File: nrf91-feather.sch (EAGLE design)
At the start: 93 parts, among them J2 CON-HEADER-1X12-MALE-PIN, J3 CON-HEADER-1X16-MALE-PIN, J4 CON-1909763-1, J5 CON-SIM-104224-0820, J6 CON-S2B-PH-SM4-TB(LF)(SN), J7 CON-1909763-1, J8 CON-USB-DX07S016JA1R1500, J9 CON-TC2030-MCP-NL, Q2 MOSFET-DUAL-COMP-SOT563, Q3 MOSFET-P-20V-4.7A-SOT23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

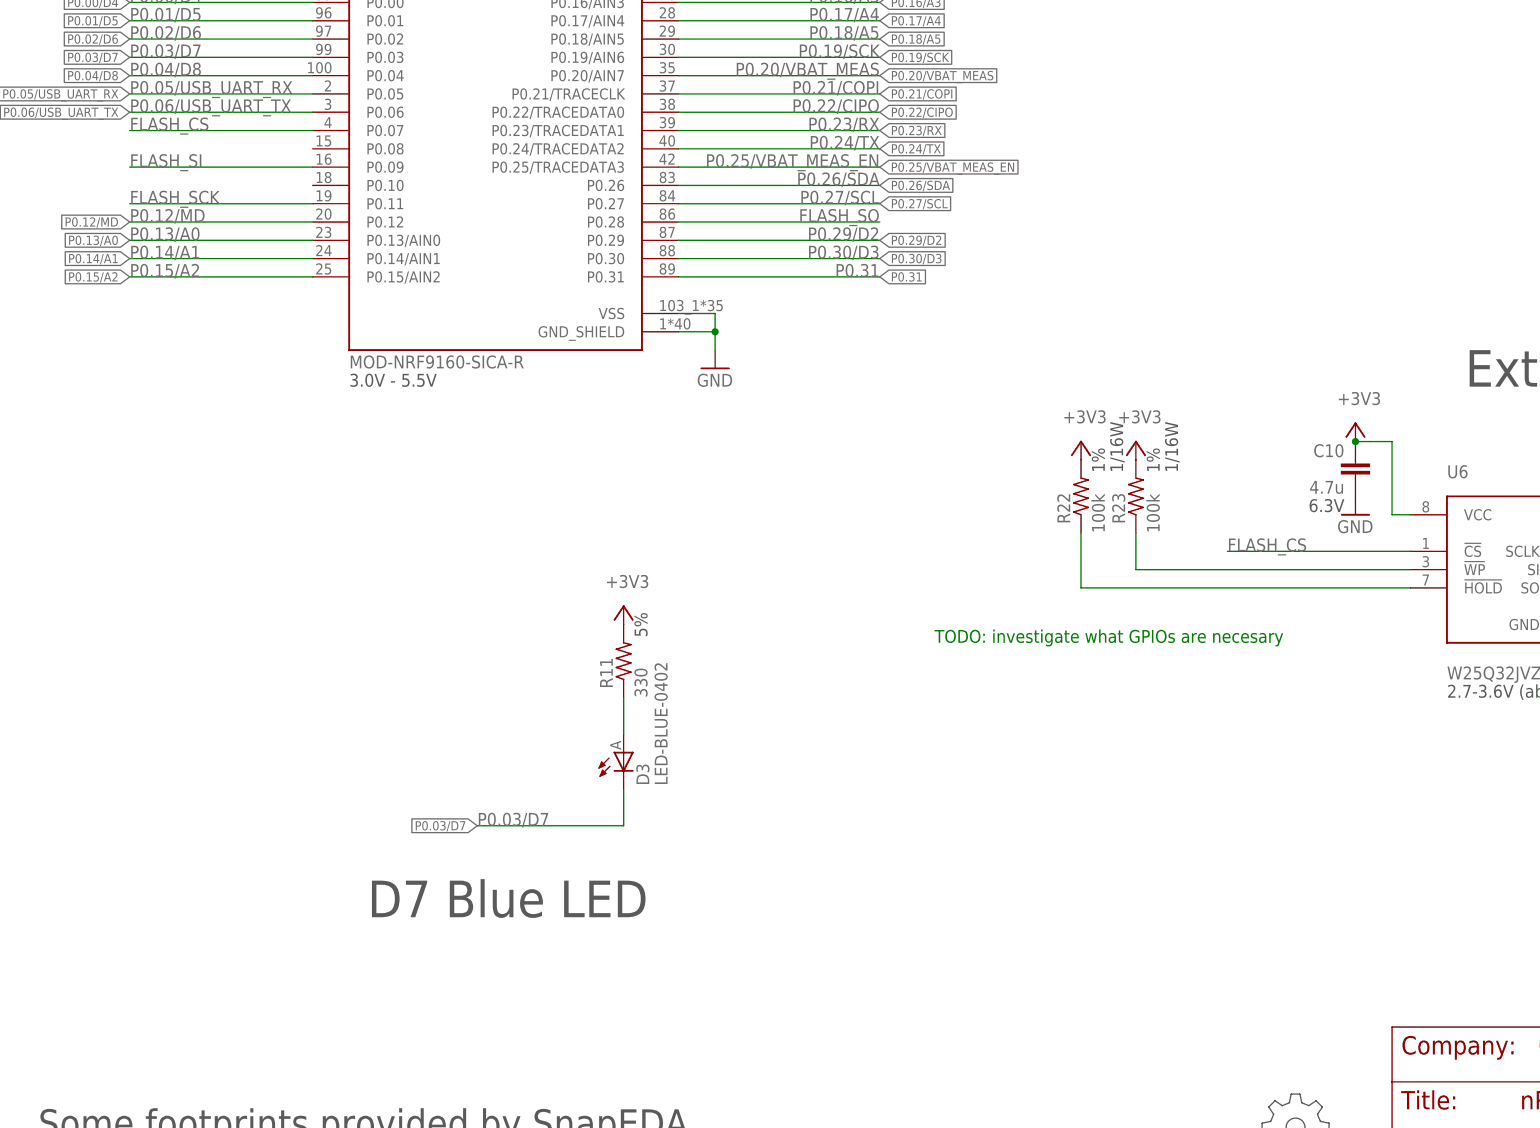
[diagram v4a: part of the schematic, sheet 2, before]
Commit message: Reconnect flash signals
Changed:
* Reconnect WP and HOLD signls
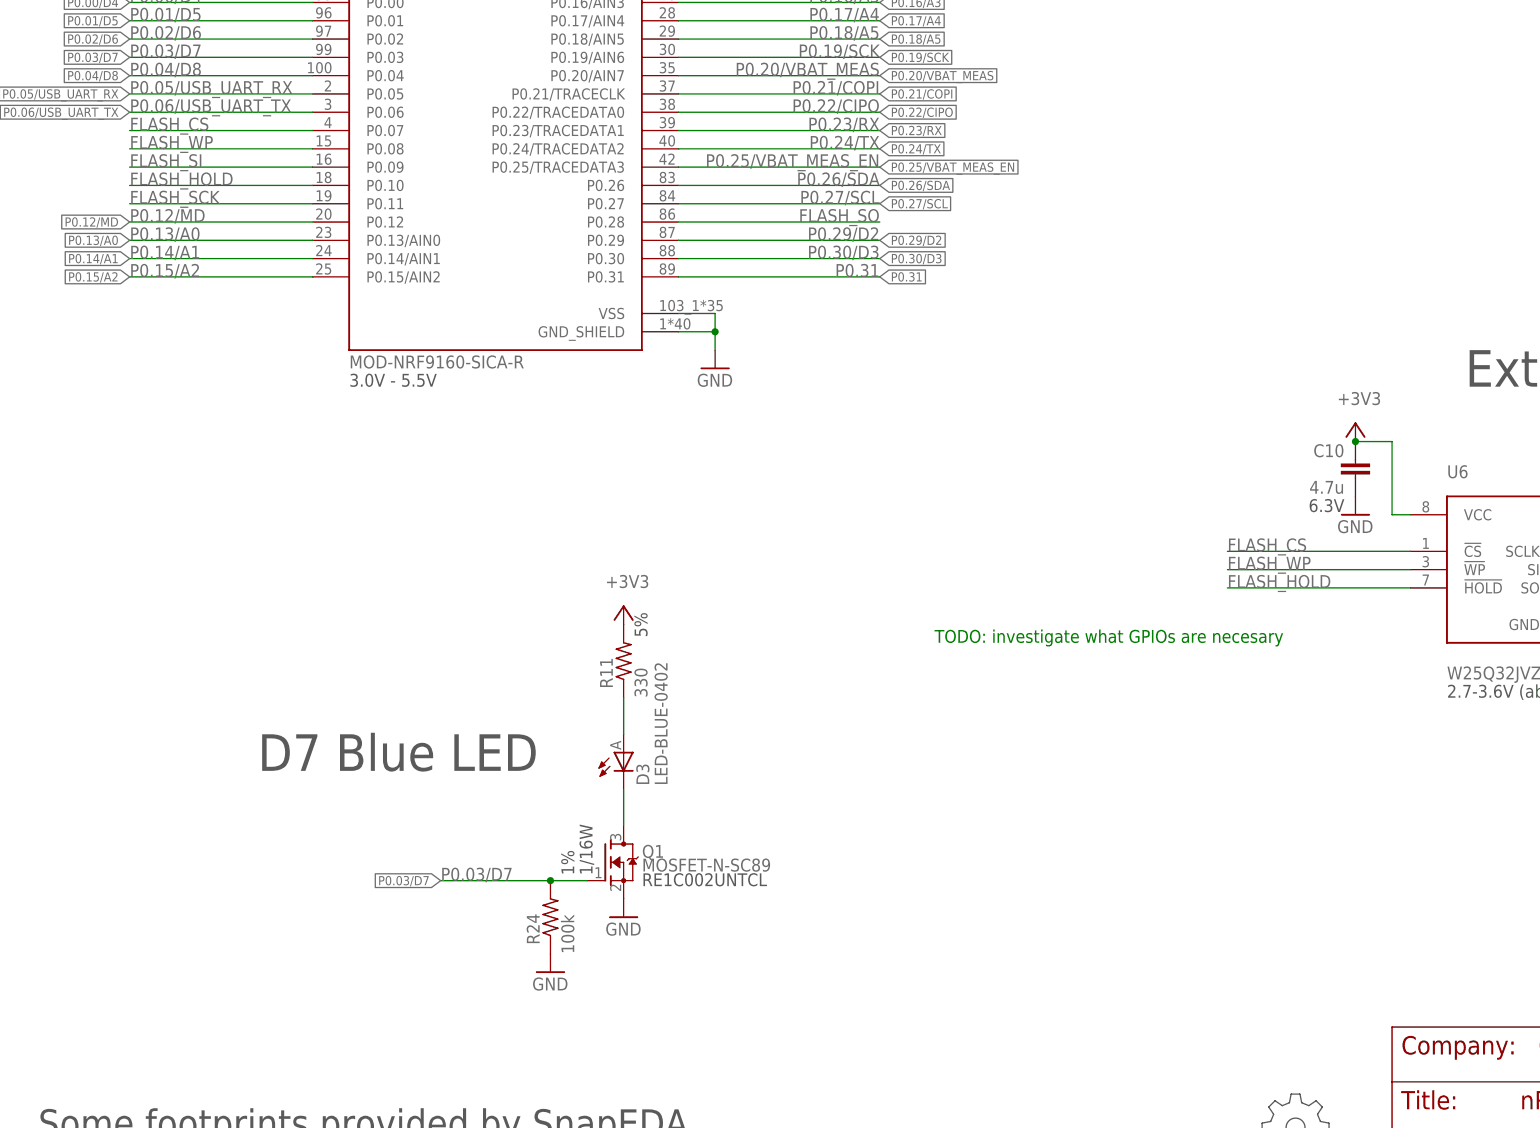
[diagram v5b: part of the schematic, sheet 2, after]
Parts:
- removed R22, R23: 100k, wolff-den:RES-100K-1%-0402
- added Q1: MOSFET-N-SC89, wolff-den:MOSFET-N-SC89
- added R24: 100k, wolff-den:RES-100K-1%-0402
- R19: value 1M -> 100k; device wolff-den:RES-1M-5%-0402 -> wolff-den:RES-100K-1%-0402
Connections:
- removed net N$14: R22.1, U6.!HOLD
- removed net N$9: R23.1, U6.!WP
- new net FLASH_HOLD: U1.P0.10, U6.!HOLD
- new net FLASH_WP: U1.P0.08, U6.!WP
- new net N$12: D3.C, Q1.D
- net +3V3: no longer R22.2, R23.2
- net GND: now also Q1.S, R24.1
- net P0.03/D7: now also Q1.G, R24.2; no longer D3.C
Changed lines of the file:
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@@
 <attribute name="MQTY" value="150"/>
 </part>
-<part name="R19" library="wolff-den" library_urn="urn:adsk.eagle:library:6370453" deviceset="RES" device="-0402" package3d_urn="urn:adsk.eagle:package:19061974/5" technology="-1M-5%" value="1M"/>
+<part name="R19" library="wolff-den" library_urn="urn:adsk.eagle:library:6370453" deviceset="RES" device="-0402" package3d_urn="urn:adsk.eagle:package:19061974/5" technology="-100K-1%" value="100k"/>
 <part name="U4" library="wolff-den" library_urn="urn:adsk.eagle:library:6370453" deviceset="POWER-SWITCH" device="-DFN4" override_package3d_urn="urn:adsk.eagle:package:36693341/2" override_package_urn="urn:adsk.eagle:footprint:36693342/1" technology="-SIP32409" value="POWER-SWITCH-SIP32409-DFN4"/>
 <part name="GND27" library="supply1" library_urn="urn:adsk.eagle:library:371" deviceset="GND" device=""/>
@@
 <part name="C6" library="wolff-den" library_urn="urn:adsk.eagle:library:6370453" deviceset="CAP" device="-0402" package3d_urn="urn:adsk.eagle:package:7419912/7" technology="-1U-25V-1" value="1u"/>
 <part name="GND47" library="supply1" library_urn="urn:adsk.eagle:library:371" deviceset="GND" device=""/>
-<part name="R22" library="wolff-den" library_urn="urn:adsk.eagle:library:6370453" deviceset="RES" device="-0402" package3d_urn="urn:adsk.eagle:package:19061974/5" technology="-100K-1%" value="100k"/>
-<part name="R23" library="wolff-den" library_urn="urn:adsk.eagle:library:6370453" deviceset="RES" device="-0402" package3d_urn="urn:adsk.eagle:package:19061974/5" technology="-100K-1%" value="100k"/>
-<part name="+3V10" library="supply1" library_urn="urn:adsk.eagle:library:371" deviceset="+3V3" device=""/>
-<part name="+3V14" library="supply1" library_urn="urn:adsk.eagle:library:371" deviceset="+3V3" device=""/>
 <part name="C3" library="wolff-den" library_urn="urn:adsk.eagle:library:6370453" deviceset="CAP" device="-0805" package3d_urn="urn:adsk.eagle:package:5807330/7" technology="-47U-6.3V" value="47u"/>
 <part name="GND11" library="supply1" library_urn="urn:adsk.eagle:library:371" deviceset="GND" device=""/>
@@
 <part name="R5" library="wolff-den" library_urn="urn:adsk.eagle:library:6370453" deviceset="RES" device="-0402" package3d_urn="urn:adsk.eagle:package:19061974/5" technology="-100K-1%" value="100k"/>
 <part name="GND32" library="supply1" library_urn="urn:adsk.eagle:library:371" deviceset="GND" device=""/>
+<part name="Q1" library="wolff-den" library_urn="urn:adsk.eagle:library:6370453" deviceset="MOSFET-N" device="-SC89" package3d_urn="urn:adsk.eagle:package:19061973/4"/>
+<part name="GND37" library="supply1" library_urn="urn:adsk.eagle:library:371" deviceset="GND" device=""/>
+<part name="R24" library="wolff-den" library_urn="urn:adsk.eagle:library:6370453" deviceset="RES" device="-0402" package3d_urn="urn:adsk.eagle:package:19061974/5" technology="-100K-1%" value="100k"/>
+<part name="GND48" library="supply1" library_urn="urn:adsk.eagle:library:371" deviceset="GND" device=""/>
 </parts>
 <sheets>
@@
 <text x="63.5" y="88.9" size="5.08" layer="97">Buttons</text>
 <text x="332.74" y="119.38" size="5.08" layer="97">External Flash</text>
-<text x="180.34" y="45.72" size="5.08" layer="97">D7 Blue LED</text>
+<text x="165.1" y="66.04" size="5.08" layer="97">D7 Blue LED</text>
 <text x="177.8" y="119.38" size="1.778" layer="97">3.0V - 5.5V</text>
 <text x="330.2" y="76.2" size="1.778" layer="97">2.7-3.6V (abs max 4.6)</text>
@@
 <attribute name="VALUE" x="248.92" y="208.28" size="1.778" layer="96" rot="MR0"/>
 </instance>
-<instance part="R22" gate="G$1" x="279.4" y="104.14" smashed="yes" rot="R90">
-<attribute name="NAME" x="277.9014" y="100.33" size="1.778" layer="95" rot="R90"/>
-<attribute name="VALUE" x="282.702" y="99.06" size="1.778" layer="96" rot="R90"/>
-<attribute name="TOLERANCE" x="282.702" y="107.442" size="1.778" layer="97" rot="R90"/>
-<attribute name="POWER" x="285.242" y="107.442" size="1.778" layer="97" rot="R90"/>
-</instance>
-<instance part="R23" gate="G$1" x="287.02" y="104.14" smashed="yes" rot="R90">
-<attribute name="NAME" x="285.5214" y="100.33" size="1.778" layer="95" rot="R90"/>
-<attribute name="VALUE" x="290.322" y="99.06" size="1.778" layer="96" rot="R90"/>
-<attribute name="TOLERANCE" x="290.322" y="107.442" size="1.778" layer="97" rot="R90"/>
-<attribute name="POWER" x="292.862" y="107.442" size="1.778" layer="97" rot="R90"/>
-</instance>
-<instance part="+3V10" gate="G$1" x="287.02" y="111.76" smashed="yes">
-<attribute name="VALUE" x="284.48" y="114.3" size="1.778" layer="96"/>
-</instance>
-<instance part="+3V14" gate="G$1" x="279.4" y="111.76" smashed="yes">
-<attribute name="VALUE" x="276.86" y="114.3" size="1.778" layer="96"/>
-</instance>
 <instance part="C3" gate="A" x="241.3" y="238.76" smashed="yes">
 <attribute name="NAME" x="242.824" y="239.141" size="1.778" layer="95"/>
@@
 <attribute name="NAME" x="148.59" y="240.1316" size="1.778" layer="95"/>
 </instance>
+<instance part="Q1" gate="A" x="213.36" y="53.34" smashed="yes">
+<attribute name="NAME" x="218.44" y="53.975" size="1.778" layer="95"/>
+<attribute name="VALUE" x="218.44" y="52.07" size="1.778" layer="96"/>
+<attribute name="MPN" x="218.44" y="50.038" size="1.778" layer="97" ratio="6"/>
+</instance>
+<instance part="GND37" gate="1" x="215.9" y="45.72" smashed="yes">
+<attribute name="VALUE" x="213.36" y="43.18" size="1.778" layer="96"/>
+</instance>
+<instance part="R24" gate="G$1" x="205.74" y="45.72" smashed="yes" rot="R90">
+<attribute name="NAME" x="204.2414" y="41.91" size="1.778" layer="95" rot="R90"/>
+<attribute name="VALUE" x="209.042" y="40.64" size="1.778" layer="96" rot="R90"/>
+<attribute name="TOLERANCE" x="209.042" y="51.562" size="1.778" layer="97" rot="R90"/>
+<attribute name="POWER" x="211.582" y="51.562" size="1.778" layer="97" rot="R90"/>
+</instance>
+<instance part="GND48" gate="1" x="205.74" y="38.1" smashed="yes">
+<attribute name="VALUE" x="203.2" y="35.56" size="1.778" layer="96"/>
+</instance>
 </instances>
 <busses>
@@
 <pinref part="GND51" gate="1" pin="GND"/>
 </segment>
+<segment>
+<pinref part="Q1" gate="A" pin="S"/>
+<pinref part="GND37" gate="1" pin="GND"/>
+</segment>
+<segment>
+<pinref part="R24" gate="G$1" pin="1"/>
+<pinref part="GND48" gate="1" pin="GND"/>
+</segment>
 </net>
 <net name="P0.12/MD" class="0">
@@
 </segment>
 <segment>
-<pinref part="R23" gate="G$1" pin="2"/>
-<pinref part="+3V10" gate="G$1" pin="+3V3"/>
-</segment>
-<segment>
-<pinref part="R22" gate="G$1" pin="2"/>
-<pinref part="+3V14" gate="G$1" pin="+3V3"/>
-</segment>
-<segment>
 <pinref part="U1" gate="G$1" pin="VDD2"/>
 <wire x1="223.52" y1="228.6" x2="228.6" y2="228.6" width="0.1524" layer="91"/>
@@
 <net name="P0.03/D7" class="0">
 <segment>
-<wire x1="195.58" y1="58.42" x2="215.9" y2="58.42" width="0.1524" layer="91"/>
-<label x="195.58" y="58.42" size="1.778" layer="95"/>
-<label x="195.58" y="58.42" size="1.27" layer="95" rot="MR0" xref="yes"/>
-<pinref part="D3" gate="G$1" pin="C"/>
-<wire x1="215.9" y1="63.5" x2="215.9" y2="58.42" width="0.1524" layer="91"/>
+<label x="190.5" y="50.8" size="1.778" layer="95"/>
+<label x="190.5" y="50.8" size="1.27" layer="95" rot="MR0" xref="yes"/>
+<wire x1="190.5" y1="50.8" x2="205.74" y2="50.8" width="0.1524" layer="91"/>
+<pinref part="R24" gate="G$1" pin="2"/>
+<pinref part="Q1" gate="A" pin="G"/>
+<wire x1="205.74" y1="50.8" x2="210.82" y2="50.8" width="0.1524" layer="91"/>
+<junction x="205.74" y="50.8"/>
 </segment>
 <segment>
@@
 </segment>
 </net>
-<net name="N$9" class="0">
-<segment>
-<pinref part="U6" gate="G$1" pin="!WP"/>
-<pinref part="R23" gate="G$1" pin="1"/>
-<wire x1="325.12" y1="93.98" x2="287.02" y2="93.98" width="0.1524" layer="91"/>
-<wire x1="287.02" y1="93.98" x2="287.02" y2="99.06" width="0.1524" layer="91"/>
-</segment>
-</net>
-<net name="N$14" class="0">
-<segment>
-<pinref part="U6" gate="G$1" pin="!HOLD"/>
-<pinref part="R22" gate="G$1" pin="1"/>
-<wire x1="325.12" y1="91.44" x2="279.4" y2="91.44" width="0.1524" layer="91"/>
-<wire x1="279.4" y1="91.44" x2="279.4" y2="99.06" width="0.1524" layer="91"/>
-</segment>
-</net>
 <net name="N$16" class="0">
 <segment>
@@
 </segment>
 </net>
+<net name="N$12" class="0">
+<segment>
+<pinref part="D3" gate="G$1" pin="C"/>
+<wire x1="215.9" y1="63.5" x2="215.9" y2="58.42" width="0.1524" layer="91"/>
+<pinref part="Q1" gate="A" pin="D"/>
+</segment>
+</net>
+<net name="FLASH_WP" class="0">
+<segment>
+<wire x1="172.72" y1="152.4" x2="147.32" y2="152.4" width="0.1524" layer="91"/>
+<label x="147.32" y="152.4" size="1.778" layer="95"/>
+<pinref part="U1" gate="G$1" pin="P0.08"/>
+</segment>
+<segment>
+<wire x1="325.12" y1="93.98" x2="299.72" y2="93.98" width="0.1524" layer="91"/>
+<label x="299.72" y="93.98" size="1.778" layer="95"/>
+<pinref part="U6" gate="G$1" pin="!WP"/>
+</segment>
+</net>
+<net name="FLASH_HOLD" class="0">
+<segment>
+<wire x1="172.72" y1="147.32" x2="147.32" y2="147.32" width="0.1524" layer="91"/>
+<label x="147.32" y="147.32" size="1.778" layer="95"/>
+<pinref part="U1" gate="G$1" pin="P0.10"/>
+</segment>
+<segment>
+<wire x1="325.12" y1="91.44" x2="299.72" y2="91.44" width="0.1524" layer="91"/>
+<label x="299.72" y="91.44" size="1.778" layer="95"/>
+<pinref part="U6" gate="G$1" pin="!HOLD"/>
+</segment>
+</net>
